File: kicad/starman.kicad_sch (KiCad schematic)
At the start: 202 parts, among them J1 M20-8771246, J10 Barrel_Jack_MountingPin, J2 M20-8770646, J3 M20-8771246, J4 ESW-106-44-T-S, J5 Conn_02x03_Counter_Clockwise, J6 ESW-112-44-T-S, J7 Conn_01x10, J8 ESW-112-44-T-S, J9 Conn_01x10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

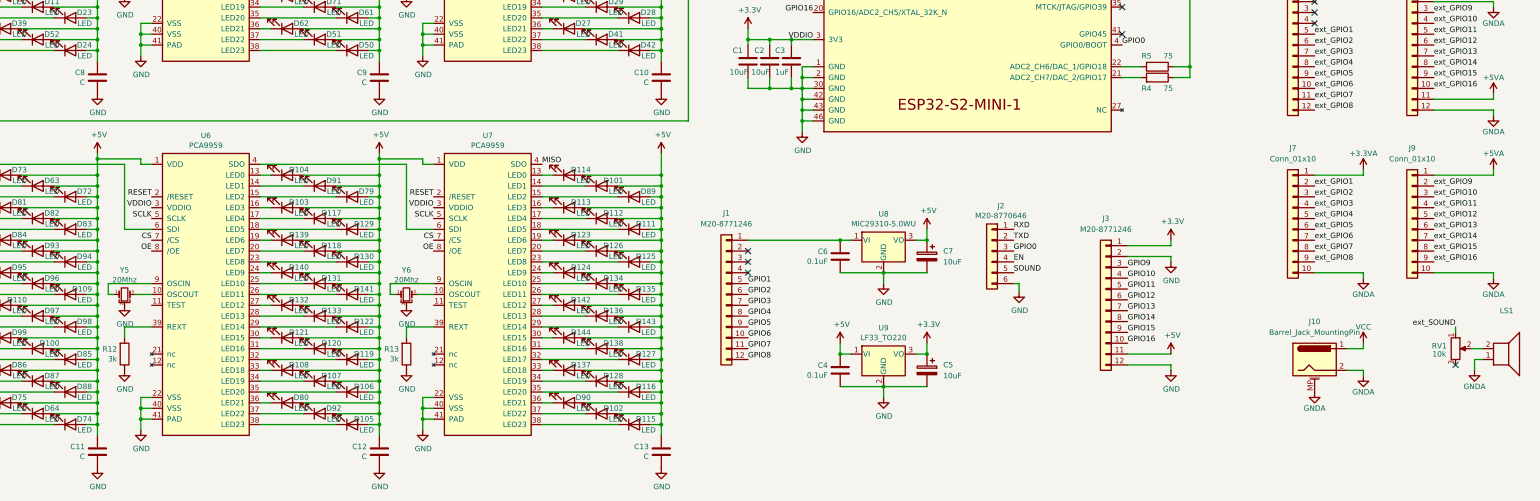
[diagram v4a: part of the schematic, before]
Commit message: Properly define caps next to the 6 PCA9959 chips
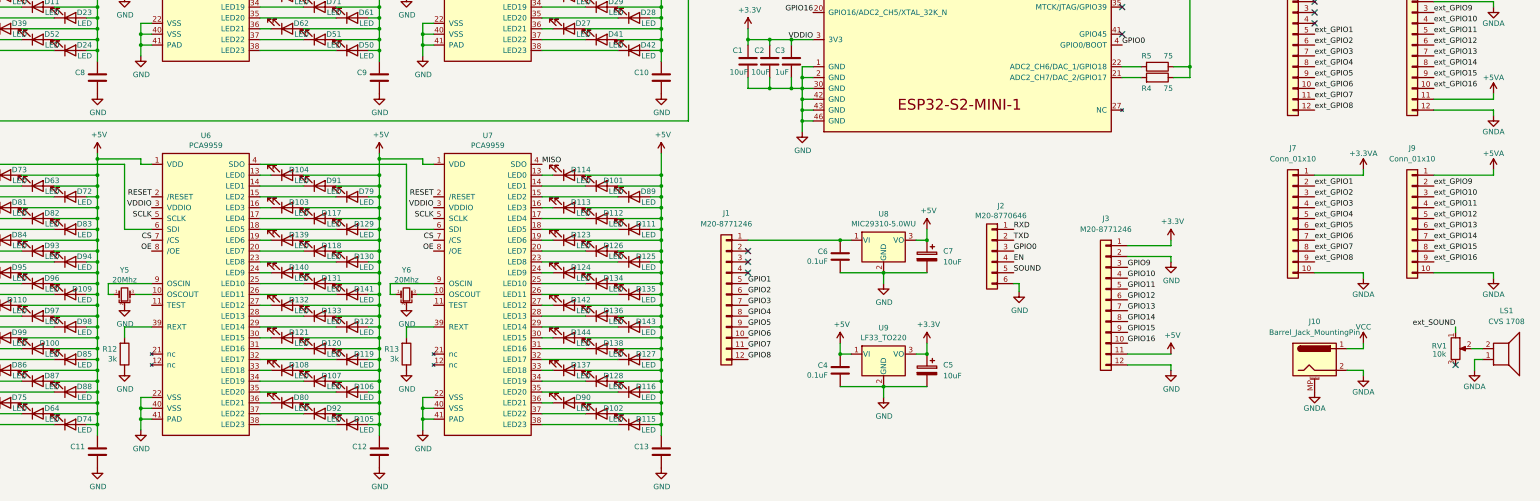
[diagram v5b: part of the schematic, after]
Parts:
- C10, C11, C12, C13, C8, C9: value C -> (none)
- LS1: value (none) -> CVS 1708; footprint (none) -> Buzzer_Beeper:MagneticBuzzer_StarMicronics_HMB-06_HMB-12
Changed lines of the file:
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@@
       (effects (font (size 1.27 1.27)) (justify right))
     )
-    (property "Value" "C" (id 1) (at 207.899 184.023 0)
+    (property "Value" "" (id 1) (at 207.899 184.023 0)
       (effects (font (size 1.27 1.27)) (justify right))
     )
@@
       (effects (font (size 1.27 1.27)) (justify right))
     )
-    (property "Value" "C" (id 1) (at 141.859 184.023 0)
+    (property "Value" "" (id 1) (at 141.859 184.023 0)
       (effects (font (size 1.27 1.27)) (justify right))
     )
@@
       (effects (font (size 1.27 1.27)) (justify right))
     )
-    (property "Value" "C" (id 1) (at 75.819 184.023 0)
+    (property "Value" "" (id 1) (at 75.819 184.023 0)
       (effects (font (size 1.27 1.27)) (justify right))
     )
@@
       (effects (font (size 1.27 1.27)) (justify right))
     )
-    (property "Value" "C" (id 1) (at 75.819 96.393 0)
+    (property "Value" "" (id 1) (at 75.819 96.393 0)
       (effects (font (size 1.27 1.27)) (justify right))
     )
@@
       (effects (font (size 1.27 1.27)) (justify right))
     )
-    (property "Value" "C" (id 1) (at 141.859 96.393 0)
+    (property "Value" "" (id 1) (at 141.859 96.393 0)
       (effects (font (size 1.27 1.27)) (justify right))
     )
@@
       (effects (font (size 1.27 1.27)) (justify right))
     )
-    (property "Value" "C" (id 1) (at 207.899 96.393 0)
+    (property "Value" "" (id 1) (at 207.899 96.393 0)
       (effects (font (size 1.27 1.27)) (justify right))
     )
@@
     (in_bom yes) (on_board yes) (fields_autoplaced)
     (property "Reference" "LS1" (id 0) (at 408.813 149.86 0))
-    (property "Value" "" (id 1) (at 408.813 152.4 0))
-    (property "Footprint" "" (id 2) (at 408.305 156.21 0)
+    (property "Value" "CVS 1708" (id 1) (at 408.813 152.4 0))
+    (property "Footprint" "Buzzer_Beeper:MagneticBuzzer_StarMicronics_HMB-06_HMB-12" (id 2) (at 408.305 156.21 0)
       (effects (font (size 1.27 1.27)) hide)
     )
@@
     )
     (path "/00000000-0000-0000-0000-000063e80e12"
-      (reference "C8") (unit 1) (value "C") (footprint "Capacitor_SMD:C_0805_2012Metric")
+      (reference "C8") (unit 1) (value "10uF") (footprint "Capacitor_SMD:C_0805_2012Metric")
     )
     (path "/00000000-0000-0000-0000-000063ebe8bc"
-      (reference "C9") (unit 1) (value "C") (footprint "Capacitor_SMD:C_0805_2012Metric")
+      (reference "C9") (unit 1) (value "10uF") (footprint "Capacitor_SMD:C_0805_2012Metric")
     )
     (path "/00000000-0000-0000-0000-000063efc5af"
-      (reference "C10") (unit 1) (value "C") (footprint "Capacitor_SMD:C_0805_2012Metric")
+      (reference "C10") (unit 1) (value "10uF") (footprint "Capacitor_SMD:C_0805_2012Metric")
     )
     (path "/00000000-0000-0000-0000-000063e43932"
-      (reference "C11") (unit 1) (value "C") (footprint "Capacitor_SMD:C_0805_2012Metric")
+      (reference "C11") (unit 1) (value "10uF") (footprint "Capacitor_SMD:C_0805_2012Metric")
     )
     (path "/00000000-0000-0000-0000-000063e0618e"
-      (reference "C12") (unit 1) (value "C") (footprint "Capacitor_SMD:C_0805_2012Metric")
+      (reference "C12") (unit 1) (value "10uF") (footprint "Capacitor_SMD:C_0805_2012Metric")
     )
     (path "/00000000-0000-0000-0000-000063dc6062"
-      (reference "C13") (unit 1) (value "C") (footprint "Capacitor_SMD:C_0805_2012Metric")
+      (reference "C13") (unit 1) (value "10uF") (footprint "Capacitor_SMD:C_0805_2012Metric")
     )
     (path "/1b6848ab-a140-4c72-bae4-c0bea42e62a7"

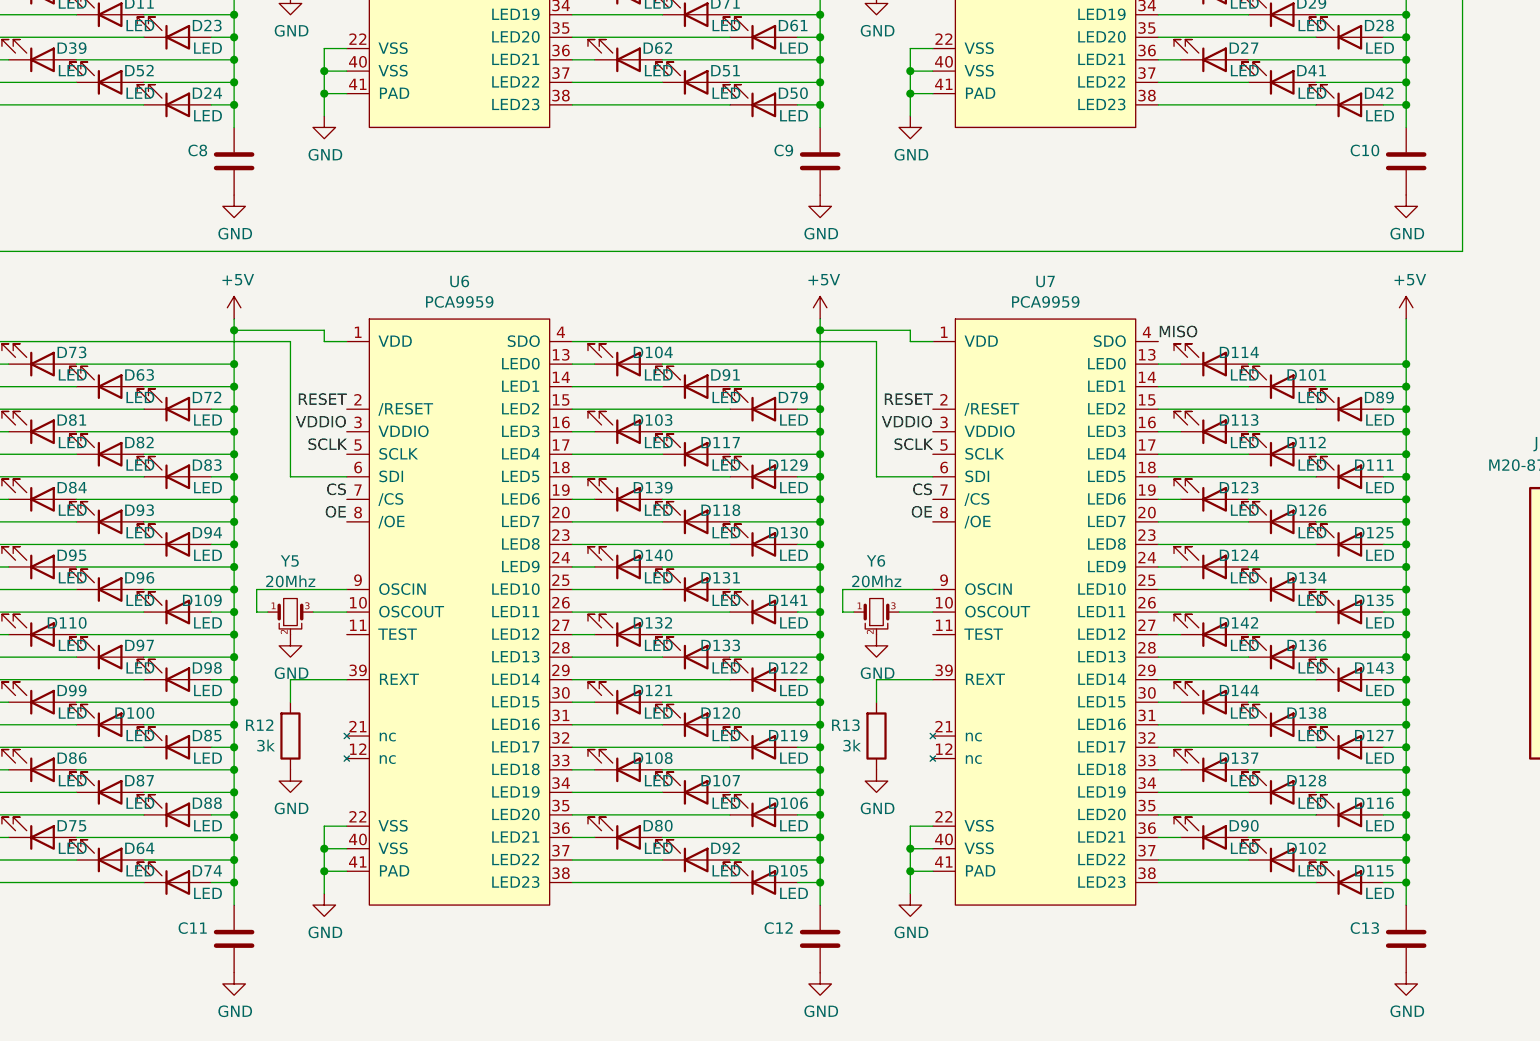
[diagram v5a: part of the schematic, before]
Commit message: Fixed DRC, restored logos, fixed github url
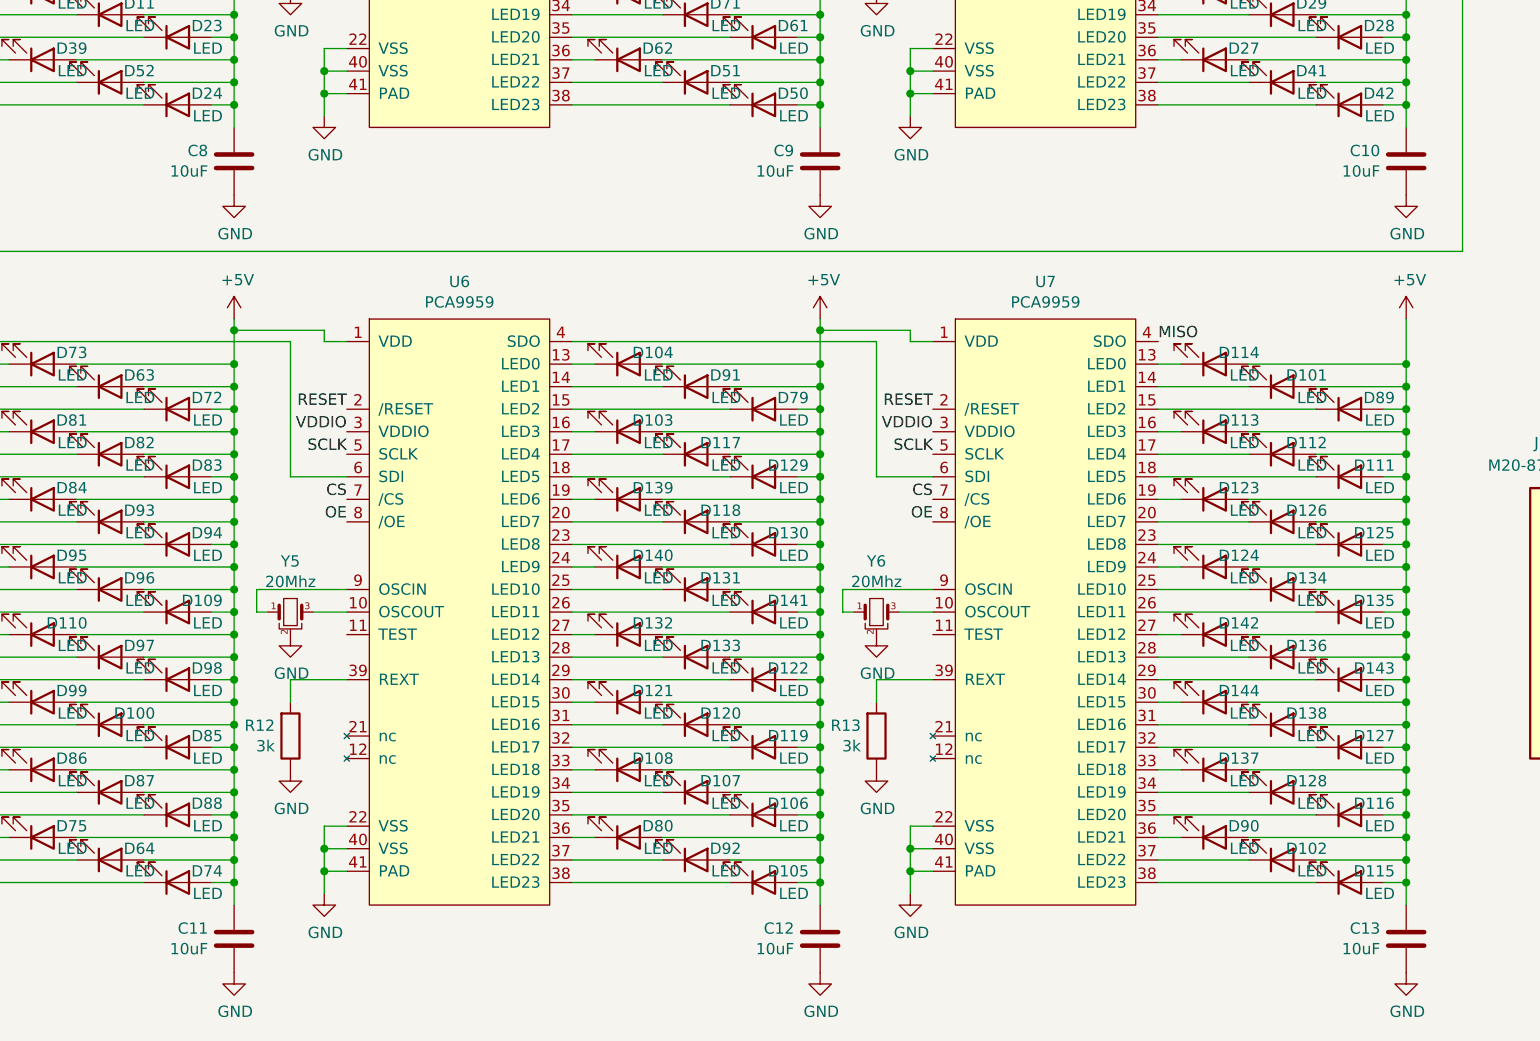
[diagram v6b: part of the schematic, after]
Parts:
- C10, C11, C12, C13, C8, C9: value (none) -> 10uF
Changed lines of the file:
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@@
       (effects (font (size 1.27 1.27)) (justify right))
     )
-    (property "Value" "" (id 1) (at 207.899 184.023 0)
+    (property "Value" "10uF" (id 1) (at 207.899 184.023 0)
       (effects (font (size 1.27 1.27)) (justify right))
     )
@@
       (effects (font (size 1.27 1.27)) (justify right))
     )
-    (property "Value" "" (id 1) (at 141.859 184.023 0)
+    (property "Value" "10uF" (id 1) (at 141.859 184.023 0)
       (effects (font (size 1.27 1.27)) (justify right))
     )
@@
       (effects (font (size 1.27 1.27)) (justify right))
     )
-    (property "Value" "" (id 1) (at 75.819 184.023 0)
+    (property "Value" "10uF" (id 1) (at 75.819 184.023 0)
       (effects (font (size 1.27 1.27)) (justify right))
     )
@@
       (effects (font (size 1.27 1.27)) (justify right))
     )
-    (property "Value" "" (id 1) (at 75.819 96.393 0)
+    (property "Value" "10uF" (id 1) (at 75.819 96.393 0)
       (effects (font (size 1.27 1.27)) (justify right))
     )
@@
       (effects (font (size 1.27 1.27)) (justify right))
     )
-    (property "Value" "" (id 1) (at 141.859 96.393 0)
+    (property "Value" "10uF" (id 1) (at 141.859 96.393 0)
       (effects (font (size 1.27 1.27)) (justify right))
     )
@@
       (effects (font (size 1.27 1.27)) (justify right))
     )
-    (property "Value" "" (id 1) (at 207.899 96.393 0)
+    (property "Value" "10uF" (id 1) (at 207.899 96.393 0)
       (effects (font (size 1.27 1.27)) (justify right))
     )

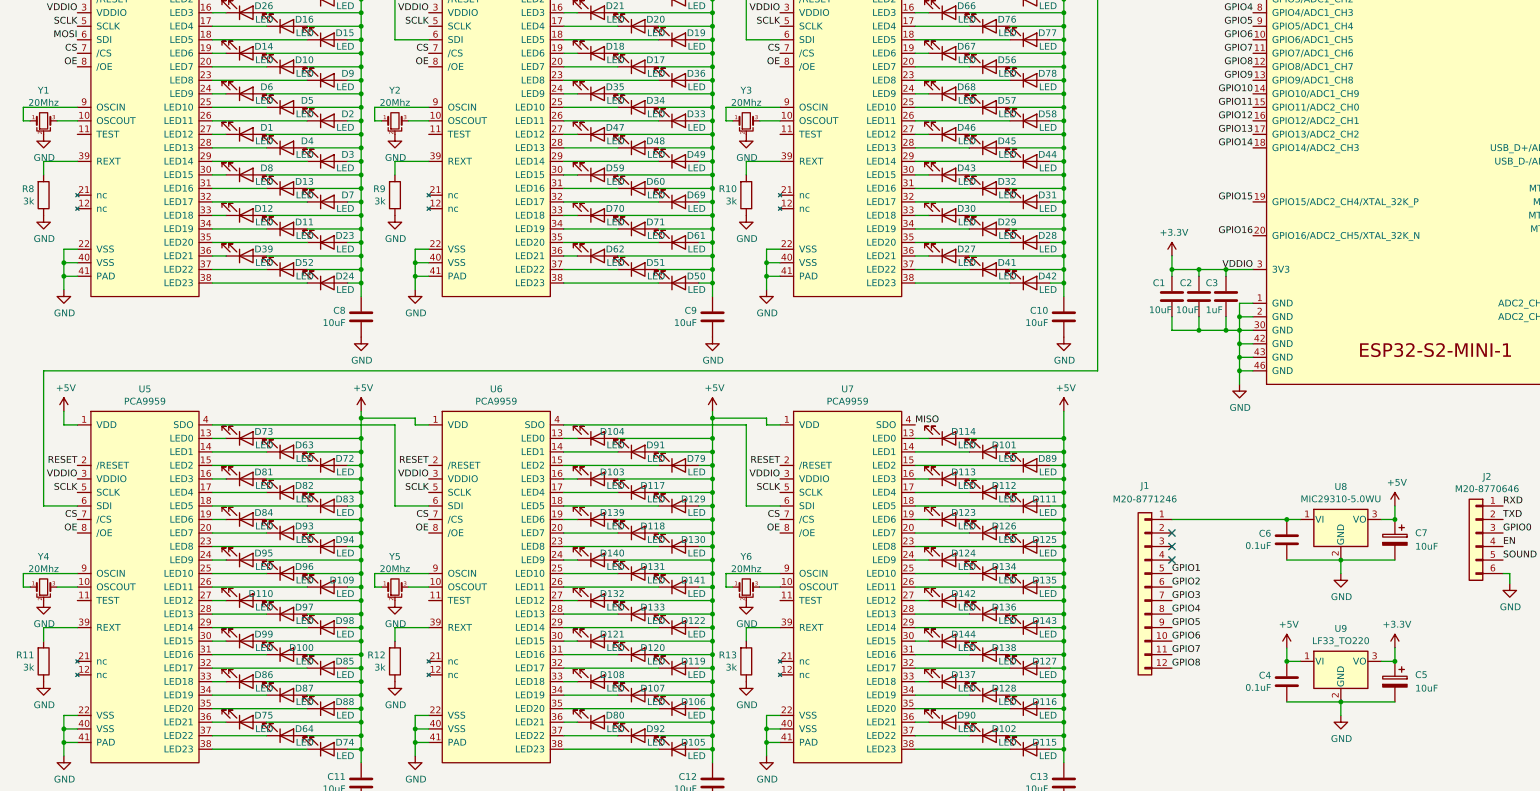
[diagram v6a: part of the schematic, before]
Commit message: Updated part numbers for Y1..Y6, U8
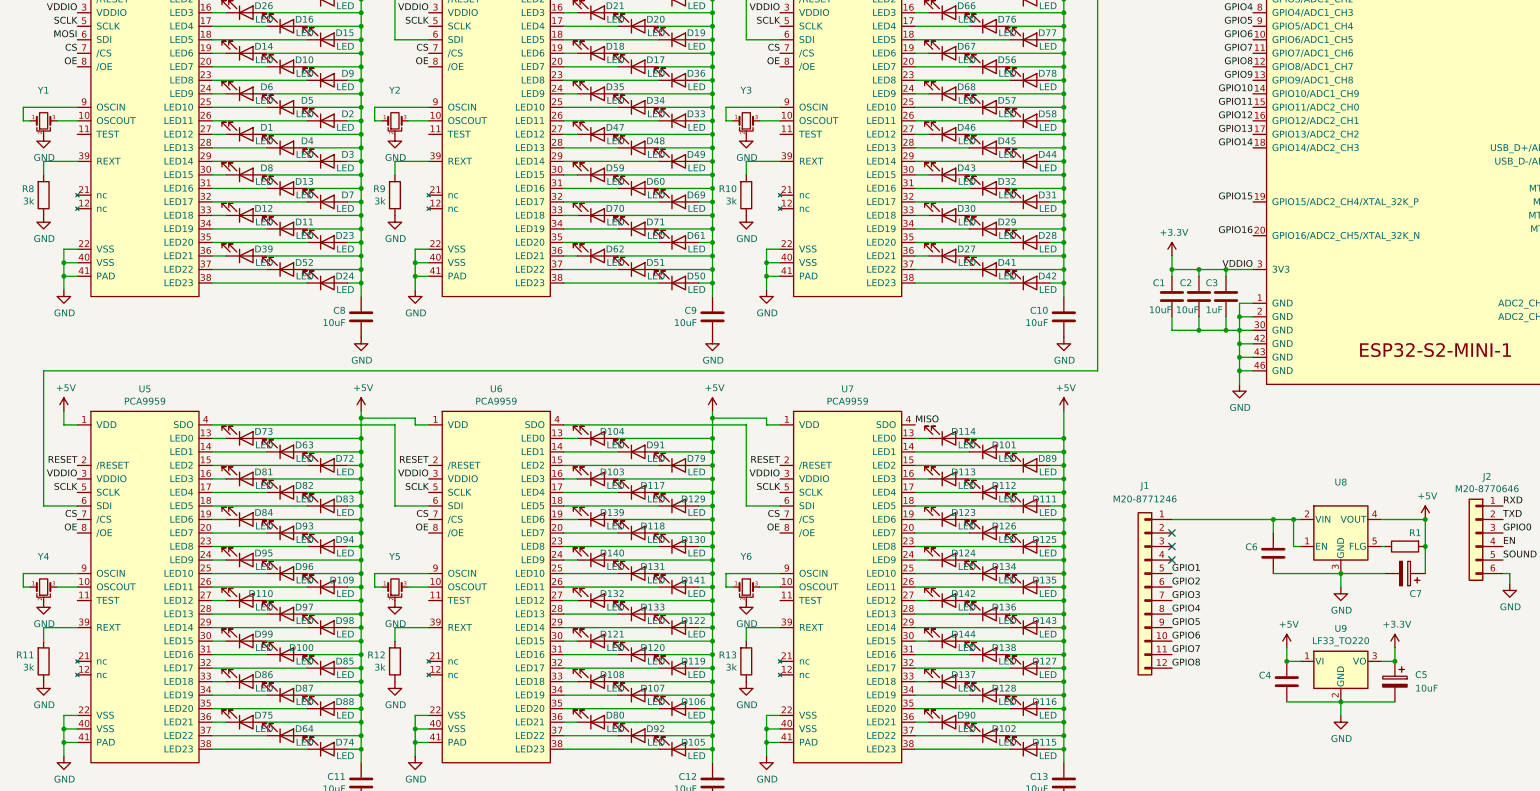
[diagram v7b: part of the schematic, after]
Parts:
- removed U8: MIC29310-5.0WU, Package_TO_SOT_SMD:TO-263-3_TabPin2, symbol Regulator_Linear:LF50_TO220
- added R1: (no value), Resistor_SMD:R_0805_2012Metric, symbol Device:R
- added U8: (no value), symbol starman:NCP59300
- C4, C6: value 0.1uF -> (none)
- C7: value 10uF -> (none)
- Y1, Y2, Y3, Y4, Y5, Y6: value 20Mhz -> (none); footprint Crystal:Resonator_SMD_muRata_CSTxExxV-3Pin_3.0x1.1mm -> (none); Part (none) -> CSTNE20M0VH3L000R0
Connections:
- net +5V: now also R1.2, U8.4 (VOUT)
- net GND: now also U8.3 (GND)
- net at C6.2, J1.1 (Pin_1): now also U8.1 (EN), U8.2 (VIN)
- new net: R1.1, U8.5 (FLG)
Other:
- moved on the sheet: C6, C7

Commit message: Minor adjustments to align with stock available.
- Adjusted J1 and J3 to be SMD headers (pin right)
- Adjusted J6 and J7 to be sockets,
- Restored R1 as part of U8
- U9 is actually TO-252-3
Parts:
- added TP1: (no value), symbol Connector:TestPoint
- C4, C6: value (none) -> 1uF
- C7: value (none) -> 47uF
- J1: value M20-8771246 -> (none); footprint Connector_PinSocket_2.54mm:PinSocket_1x12_P2.54mm_Vertical_SMD_Pin1Right -> (none)
- J2: value M20-8770646 -> (none); footprint Connector_PinSocket_2.54mm:PinSocket_1x06_P2.54mm_Vertical_SMD_Pin1Left -> (none)
- J3: value M20-8771246 -> (none); footprint Connector_PinSocket_2.54mm:PinSocket_1x12_P2.54mm_Vertical_SMD_Pin1Left -> (none)
- J4: value ESW-106-44-T-S -> (none); footprint Connector_PinHeader_2.54mm:PinHeader_1x06_P2.54mm_Vertical -> (none)
- J6: value ESW-112-44-T-S -> (none); footprint Connector_PinHeader_2.54mm:PinHeader_1x12_P2.54mm_Vertical -> (none); Vendor M20-8771246 -> (none)
- J8: value ESW-112-44-T-S -> (none); footprint Connector_PinHeader_2.54mm:PinHeader_1x12_P2.54mm_Vertical -> (none)
- R1: value (none) -> 100k
- U8: value (none) -> NCP59301; footprint (none) -> Package_TO_SOT_SMD:TO-263-5_TabPin3
- U9: value LF33_TO220 -> LF33; footprint Package_TO_SOT_SMD:SOT-223-3_TabPin2 -> Package_TO_SOT_SMD:TO-252-3_TabPin2
- Y1, Y2, Y3, Y4, Y5, Y6: value (none) -> 20Mhz; footprint (none) -> Crystal:Resonator_SMD_muRata_CSTxExxV-3Pin_3.0x1.1mm
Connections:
- net at R1.1, U8.5 (FLG): now also TP1.1
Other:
- moved on the sheet: C6, C7, J2
